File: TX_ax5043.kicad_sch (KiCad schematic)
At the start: 31 parts, among them J7 2118714-2, P6 CONUFL001-SMD-T, P7 CONUFL001-SMD-T, Q7 DMP2037U, U23 AX5043

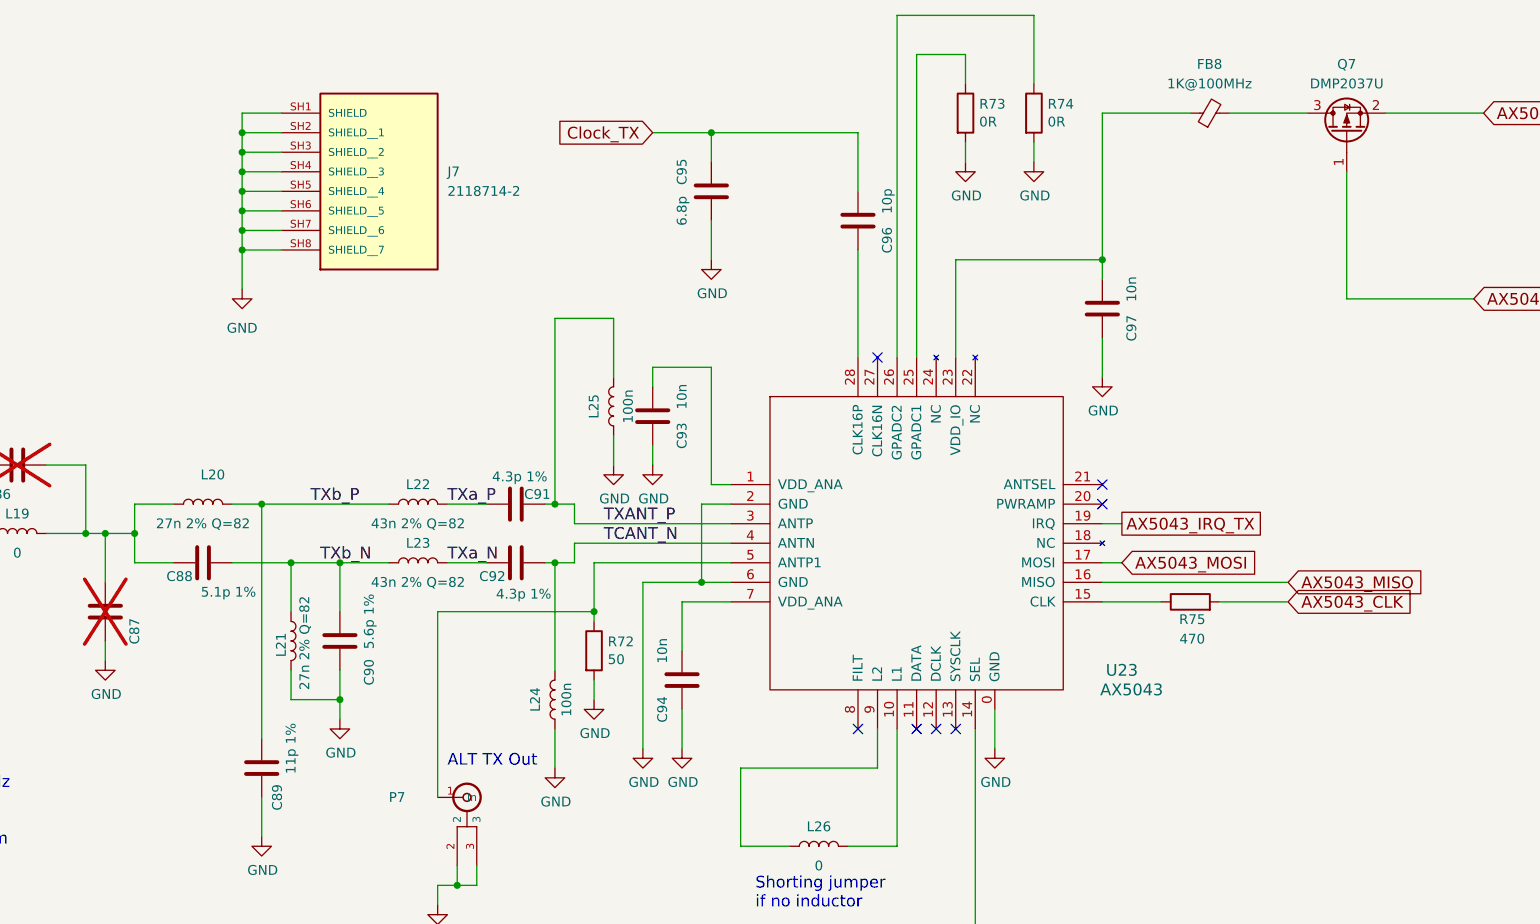
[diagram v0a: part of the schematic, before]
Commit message: Lots of updates to ease manufacturing
Component changes, changes in the formatting of the values, etc.

Signed-off-by: Corey Minyard <corey@minyard.net>
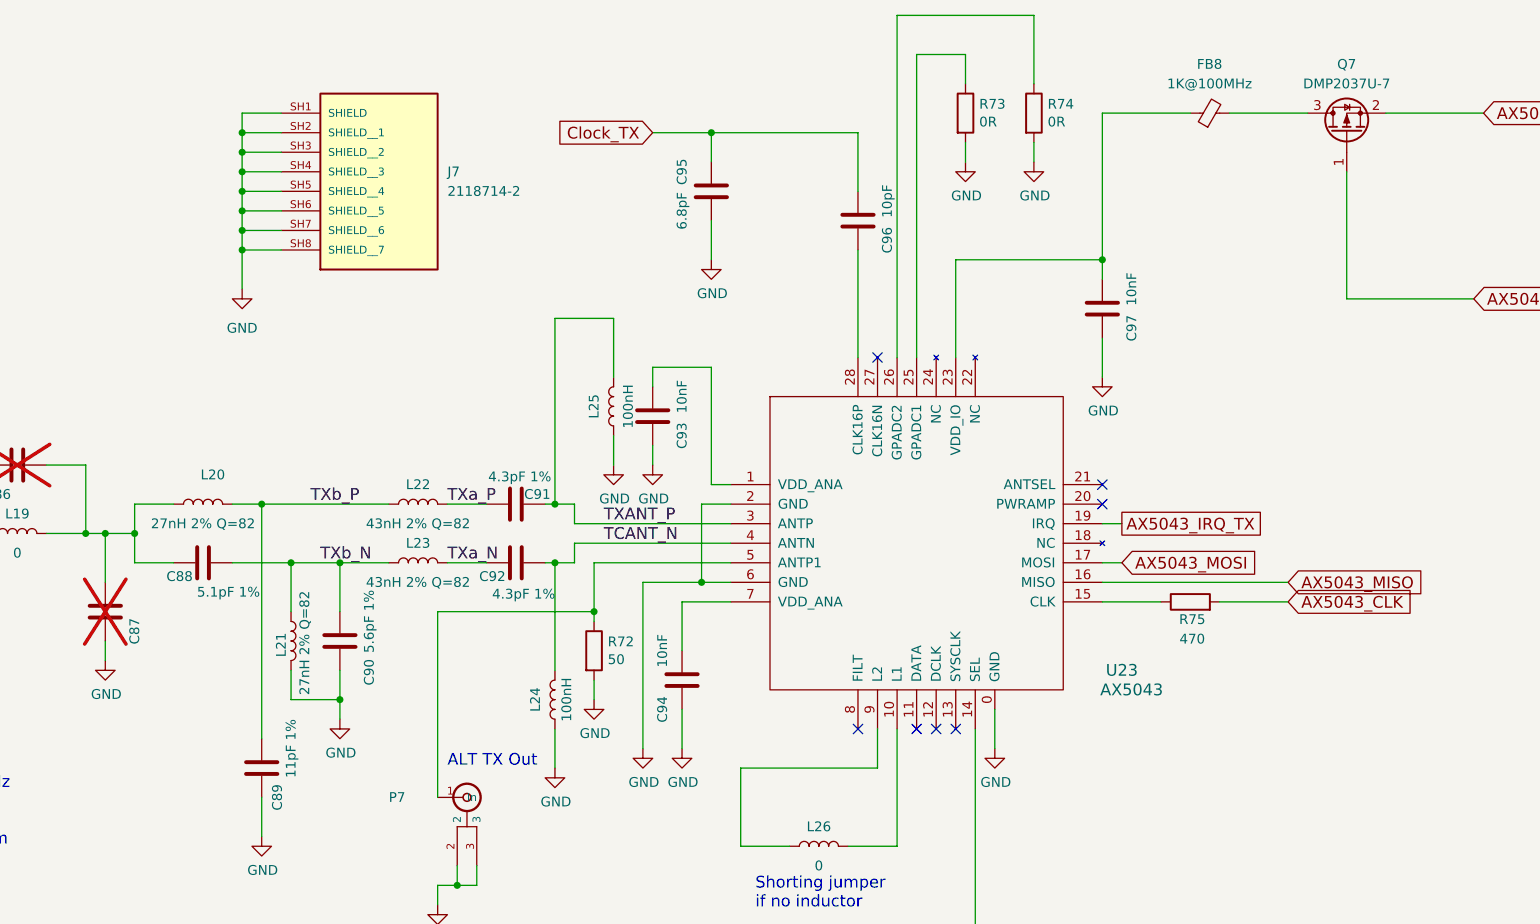
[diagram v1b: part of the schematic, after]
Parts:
- C88: value 5.1p 1% -> 5.1pF 1%
- C89: value 11p 1% -> 11pF 1%
- C90: value 5.6p 1% -> 5.6pF 1%
- C91, C92: value 4.3p 1% -> 4.3pF 1%
- C93, C94, C97: value 10n -> 10nF
- C95: value 6.8p -> 6.8pF
- C96: value 10p -> 10pF
- L20, L21: value 27n 2% Q=82 -> 27nH 2% Q=82
- L22, L23: value 43n 2% Q=82 -> 43nH 2% Q=82
- L24, L25: value 100n -> 100nH
- Q7: value DMP2037U -> DMP2037U-7
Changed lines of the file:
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@@
 			)
 		)
-		(property "Value" "4.3p 1%"
+		(property "Value" "4.3pF 1%"
 			(at 213.868 128.524 90)
 			(effects
@@
 			)
 		)
-		(property "Value" "4.3p 1%"
+		(property "Value" "4.3pF 1%"
 			(at 214.376 143.764 90)
 			(effects
@@
 			)
 		)
-		(property "Value" "10n"
+		(property "Value" "10nF"
 			(at 234.95 118.11 90)
 			(effects
@@
 			)
 		)
-		(property "Value" "10n"
+		(property "Value" "10nF"
 			(at 293.37 104.14 90)
 			(effects
@@
 			)
 		)
-		(property "Value" "5.6p 1%"
+		(property "Value" "5.6pF 1%"
 			(at 194.31 147.32 90)
 			(effects
@@
 			)
 		)
-		(property "Value" "27n 2% Q=82"
+		(property "Value" "27nH 2% Q=82"
 			(at 185.928 150.114 90)
 			(effects
@@
 			)
 		)
-		(property "Value" "5.1p 1%"
+		(property "Value" "5.1pF 1%"
 			(at 176.022 143.51 90)
 			(effects
@@
 			)
 		)
-		(property "Value" "11p 1%"
+		(property "Value" "11pF 1%"
 			(at 184.15 163.83 90)
 			(effects
@@
 			)
 		)
-		(property "Value" "10n"
+		(property "Value" "10nF"
 			(at 232.41 151.13 90)
 			(effects
@@
 			)
 		)
-		(property "Value" "10p"
+		(property "Value" "10pF"
 			(at 261.62 92.71 90)
 			(effects
@@
 			)
 		)
-		(property "Value" "43n 2% Q=82"
+		(property "Value" "43nH 2% Q=82"
 			(at 200.66 142.24 90)
 			(effects
@@
 			)
 		)
-		(property "Value" "100n"
+		(property "Value" "100nH"
 			(at 227.965 119.38 90)
 			(effects
@@
 			)
 		)
-		(property "Value" "43n 2% Q=82"
+		(property "Value" "43nH 2% Q=82"
 			(at 200.66 134.62 90)
 			(effects
@@
 			)
 		)
-		(property "Value" "100n"
+		(property "Value" "100nH"
 			(at 219.964 157.48 90)
 			(effects
@@
 			)
 		)
-		(property "Value" "6.8p"
+		(property "Value" "6.8pF"
 			(at 234.95 93.98 90)
 			(effects
@@
 			)
 		)
-		(property "Value" "27n 2% Q=82"
+		(property "Value" "27nH 2% Q=82"
 			(at 172.72 134.62 90)
 			(effects
@@
 			)
 		)
-		(property "Value" "DMP2037U"
+		(property "Value" "DMP2037U-7"
 			(at 321.31 77.47 90)
 			(effects

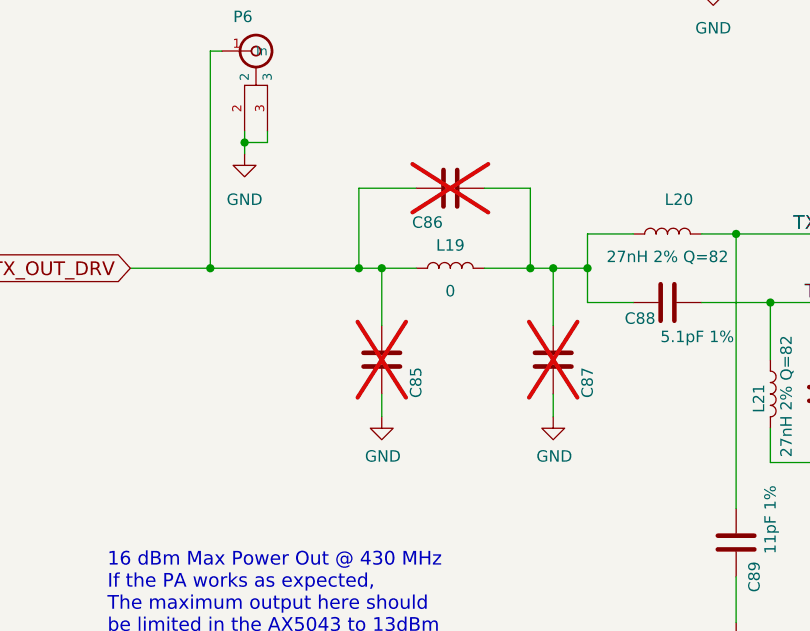
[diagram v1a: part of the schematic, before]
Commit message: Replace the LNA output filter with discretes
These take up some more room, but are much cheaper and perform
quite a bit better.

Signed-off-by: Corey Minyard <corey@minyard.net>
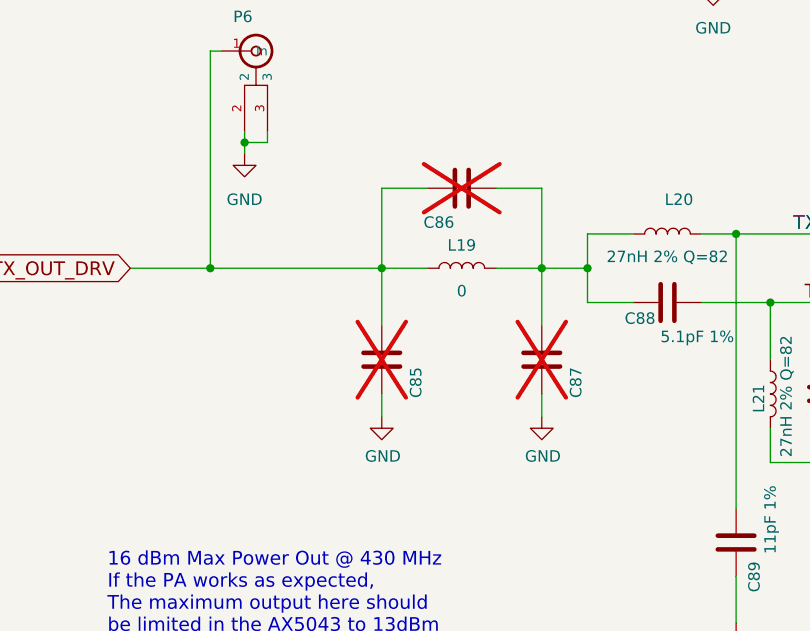
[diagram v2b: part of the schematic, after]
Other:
- moved on the sheet: C86, C87, L19
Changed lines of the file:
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@@
 	)
 	(junction
-		(at 138.43 135.89)
-		(diameter 0)
-		(color 0 0 0 0)
-	)
-	(junction
 		(at 190.5 139.7)
 		(diameter 0)
@@
 	)
 	(junction
-		(at 157.48 135.89)
-		(diameter 0)
-		(color 0 0 0 0)
-	)
-	(junction
 		(at 121.92 135.89)
 		(diameter 0)
@@
 	)
 	(junction
-		(at 160.02 135.89)
-		(diameter 0)
-		(color 0 0 0 0)
-	)
-	(junction
 		(at 177.8 93.98)
 		(diameter 0)
@@
 	)
 	(junction
+		(at 158.75 135.89)
+		(diameter 0)
+		(color 0 0 0 0)
+	)
+	(junction
 		(at 163.83 135.89)
 		(diameter 0)
@@
 	(wire
 		(pts
-			(xy 160.02 149.86) (xy 160.02 152.4)
+			(xy 158.75 149.86) (xy 158.75 152.4)
 		)
 		(stroke
@@
 	(wire
 		(pts
-			(xy 138.43 135.89) (xy 140.97 135.89)
-		)
-		(stroke
-			(width 0)
-			(type default)
-		)
-	)
-	(wire
-		(pts
 			(xy 204.47 139.7) (xy 209.55 139.7)
 		)
@@
 	(wire
 		(pts
-			(xy 144.78 127) (xy 138.43 127)
+			(xy 146.05 127) (xy 140.97 127)
 		)
 		(stroke
@@
 	(wire
 		(pts
-			(xy 160.02 142.24) (xy 160.02 135.89)
+			(xy 158.75 142.24) (xy 158.75 135.89)
 		)
 		(stroke
@@
 	(wire
 		(pts
-			(xy 152.4 127) (xy 157.48 127)
+			(xy 153.67 127) (xy 158.75 127)
 		)
 		(stroke
@@
 	(wire
 		(pts
+			(xy 158.75 135.89) (xy 163.83 135.89)
+		)
+		(stroke
+			(width 0)
+			(type default)
+		)
+	)
+	(wire
+		(pts
 			(xy 242.57 166.37) (xy 242.57 176.53)
 		)
@@
 	(wire
 		(pts
-			(xy 157.48 127) (xy 157.48 135.89)
+			(xy 158.75 127) (xy 158.75 135.89)
 		)
 		(stroke
@@
 	(wire
 		(pts
-			(xy 140.97 135.89) (xy 144.78 135.89)
+			(xy 140.97 135.89) (xy 146.05 135.89)
 		)
 		(stroke
@@
 	(wire
 		(pts
-			(xy 152.4 135.89) (xy 157.48 135.89)
+			(xy 153.67 135.89) (xy 158.75 135.89)
 		)
 		(stroke
@@
 	(wire
 		(pts
-			(xy 160.02 135.89) (xy 163.83 135.89)
-		)
-		(stroke
-			(width 0)
-			(type default)
-		)
-	)
-	(wire
-		(pts
 			(xy 177.8 83.82) (xy 182.88 83.82)
 		)
@@
 	(wire
 		(pts
-			(xy 138.43 127) (xy 138.43 135.89)
+			(xy 140.97 127) (xy 140.97 135.89)
 		)
 		(stroke
@@
 	(wire
 		(pts
-			(xy 157.48 135.89) (xy 160.02 135.89)
-		)
-		(stroke
-			(width 0)
-			(type default)
-		)
-	)
-	(wire
-		(pts
 			(xy 177.8 99.06) (xy 182.88 99.06)
 		)
@@
 	(wire
 		(pts
-			(xy 121.92 135.89) (xy 138.43 135.89)
+			(xy 121.92 135.89) (xy 140.97 135.89)
 		)
 		(stroke
@@
 	(symbol
 		(lib_id "Device:C")
-		(at 148.59 127 270)
+		(at 149.86 127 270)
 		(unit 1)
 		(exclude_from_sim no)
@@
 		(dnp yes)
 		(property "Reference" "C86"
-			(at 146.05 130.81 90)
+			(at 147.32 130.81 90)
 			(effects
 				(font
@@
 		)
 		(property "Value" "~"
-			(at 148.59 127 90)
+			(at 149.86 127 90)
 			(effects
 				(font
@@
 		)
 		(property "Footprint" "Capacitor_SMD:C_0402_1005Metric_Pad0.74x0.62mm_HandSolder"
-			(at 144.78 127.9652 0)
+			(at 146.05 127.9652 0)
 			(effects
 				(font
@@
 		)
 		(property "Datasheet" "~"
-			(at 148.59 127 0)
+			(at 149.86 127 0)
 			(effects
 				(font
@@
 		)
 		(property "Description" ""
-			(at 148.59 127 0)
+			(at 149.86 127 0)
 			(effects
 				(font
@@
 	(symbol
 		(lib_id "Device:C")
-		(at 160.02 146.05 0)
+		(at 158.75 146.05 0)
 		(unit 1)
 		(exclude_from_sim no)
@@
 		(dnp yes)
 		(property "Reference" "C87"
-			(at 163.83 148.59 90)
+			(at 162.56 148.59 90)
 			(effects
 				(font
@@
 		)
 		(property "Value" "~"
-			(at 163.83 143.51 90)
+			(at 162.56 143.51 90)
 			(effects
 				(font
@@
 		)
 		(property "Footprint" "Capacitor_SMD:C_0402_1005Metric_Pad0.74x0.62mm_HandSolder"
-			(at 160.9852 149.86 0)
+			(at 159.7152 149.86 0)
 			(effects
 				(font
@@
 		)
 		(property "Datasheet" "~"
-			(at 160.02 146.05 0)
+			(at 158.75 146.05 0)
 			(effects
 				(font
@@
 		)
 		(property "Description" ""
-			(at 160.02 146.05 0)
+			(at 158.75 146.05 0)
 			(effects
 				(font
@@
 	(symbol
 		(lib_id "power:GND")
-		(at 160.02 152.4 0)
+		(at 158.75 152.4 0)
 		(unit 1)
 		(exclude_from_sim no)
@@
 		(dnp no)
 		(property "Reference" "#PWR0186"
-			(at 160.02 158.75 0)
+			(at 158.75 158.75 0)
 			(effects
 				(font
@@
 		)
 		(property "Value" "GND"
-			(at 160.147 156.7942 0)
+			(at 158.877 156.7942 0)
 			(effects
 				(font
@@
 		)
 		(property "Footprint" ""
-			(at 160.02 152.4 0)
+			(at 158.75 152.4 0)
 			(effects
 				(font
@@
 		)
 		(property "Datasheet" ""
-			(at 160.02 152.4 0)
+			(at 158.75 152.4 0)
 			(effects
 				(font
@@
 		)
 		(property "Description" ""
-			(at 160.02 152.4 0)
+			(at 158.75 152.4 0)
 			(effects
 				(font
@@
 	(symbol
 		(lib_id "Device:L")
-		(at 148.59 135.89 90)
+		(at 149.86 135.89 90)
 		(unit 1)
 		(exclude_from_sim no)
@@
 		(dnp no)
 		(property "Reference" "L19"
-			(at 148.59 133.35 90)
+			(at 149.86 133.35 90)
 			(effects
 				(font
@@
 		)
 		(property "Value" "0"
-			(at 148.59 138.43 90)
+			(at 149.86 138.43 90)
 			(effects
 				(font
@@
 		)
 		(property "Footprint" "Inductor_SMD:L_0603_1608Metric_Pad1.05x0.95mm_HandSolder"
-			(at 148.59 135.89 0)
+			(at 149.86 135.89 0)
 			(effects
 				(font
@@
 		)
 		(property "Datasheet" "~"
-			(at 148.59 135.89 0)
+			(at 149.86 135.89 0)
 			(effects
 				(font
@@
 		)
 		(property "Description" ""
-			(at 148.59 135.89 0)
+			(at 149.86 135.89 0)
 			(effects
 				(font

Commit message: Update all resistors to have an ohm symbol
Make it more clean in the BOM what they are.

Signed-off-by: Corey Minyard <corey@minyard.net>
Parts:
- R72: value 50 -> 50Ω
- R75: value 470 -> 470Ω
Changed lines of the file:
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@@
 			)
 		)
-		(property "Value" "50"
+		(property "Value" "50Ω"
 			(at 225.298 152.273 0)
 			(effects
@@
 			)
 		)
-		(property "Value" "470"
+		(property "Value" "470Ω"
 			(at 301.244 149.606 90)
 			(effects

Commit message: Massive rework of filtering and inductors
Now that I know how inductors really work.

Signed-off-by: Corey Minyard <corey@minyard.net>
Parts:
- L20, L21: value 27nH 2% Q=82 -> 27nH 2%
- L22, L23: value 43nH 2% Q=82 -> 43nH 2%
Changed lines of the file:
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@@
 			)
 		)
-		(property "Value" "27nH 2% Q=82"
+		(property "Value" "27nH 2%"
 			(at 185.928 150.114 90)
 			(effects
@@
 			)
 		)
-		(property "Value" "43nH 2% Q=82"
+		(property "Value" "43nH 2%"
 			(at 200.66 142.24 90)
 			(effects
@@
 			)
 		)
-		(property "Value" "43nH 2% Q=82"
+		(property "Value" "43nH 2%"
 			(at 200.66 134.62 90)
 			(effects
@@
 			)
 		)
-		(property "Value" "27nH 2% Q=82"
+		(property "Value" "27nH 2%"
 			(at 172.72 134.62 90)
 			(effects

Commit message: Have the BOM file fixer output xls, not csv
The omega symbol gets translated properly from xls.

Signed-off-by: Corey Minyard <corey@minyard.net>
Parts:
- FB8: footprint Resistor_SMD:R_0603_1608Metric_Pad0.98x0.95mm_HandSolder -> Inductor_SMD:L_0603_1608Metric_Pad1.05x0.95mm_HandSolder
- R73, R74: value 0R -> 0Ω
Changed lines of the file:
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@@
 			)
 		)
-		(property "Value" "0R"
+		(property "Value" "0Ω"
 			(at 273.558 82.423 0)
 			(effects
@@
 			)
 		)
-		(property "Value" "0R"
+		(property "Value" "0Ω"
 			(at 282.448 82.423 0)
 			(effects
@@
 			)
 		)
-		(property "Footprint" "Resistor_SMD:R_0603_1608Metric_Pad0.98x0.95mm_HandSolder"
+		(property "Footprint" "Inductor_SMD:L_0603_1608Metric_Pad1.05x0.95mm_HandSolder"
 			(at 303.53 83.058 90)
 			(effects

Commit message: Minor fixes for BOM values
Signed-off-by: Corey Minyard <corey@minyard.net>
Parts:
- FB8: value 1K@100MHz -> 1KΩ@100MHz
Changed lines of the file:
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@@
 			)
 		)
-		(property "Value" "1K@100MHz"
+		(property "Value" "1KΩ@100MHz"
 			(at 303.4919 77.47 90)
 			(effects

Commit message: Added some docs and notes about various things
Signed-off-by: Corey Minyard <corey@minyard.net>
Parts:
- C85, C86, C87: now left out of the parts list
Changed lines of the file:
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@@
 		(unit 1)
 		(exclude_from_sim no)
-		(in_bom yes)
+		(in_bom no)
 		(on_board yes)
 		(dnp yes)
@@
 		(unit 1)
 		(exclude_from_sim no)
-		(in_bom yes)
+		(in_bom no)
 		(on_board yes)
 		(dnp yes)
@@
 		(unit 1)
 		(exclude_from_sim no)
-		(in_bom yes)
+		(in_bom no)
 		(on_board yes)
 		(dnp yes)

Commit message: A bunch of work on component selections
And little fixups for things I found.

Signed-off-by: Corey Minyard <corey@minyard.net>
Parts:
- C88: value 5.1pF 1% -> 5.1pF ±.1
- C90: value 5.6pF 1% -> 5.6pF ±.1
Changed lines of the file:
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@@
 		(dnp no)
 		(property "Reference" "C90"
-			(at 194.31 153.924 90)
-			(effects
-				(font
-					(size 1.27 1.27)
-				)
-			)
-		)
-		(property "Value" "5.6pF 1%"
+			(at 194.31 154.94 90)
+			(effects
+				(font
+					(size 1.27 1.27)
+				)
+			)
+		)
+		(property "Value" "5.6pF ±.1"
 			(at 194.31 147.32 90)
 			(effects
@@
 			)
 		)
-		(property "Value" "5.1pF 1%"
-			(at 176.022 143.51 90)
-			(effects
-				(font
+		(property "Value" "5.1pF ±.1"
+			(at 173.482 143.764 90)
+			(effects
+				(font
